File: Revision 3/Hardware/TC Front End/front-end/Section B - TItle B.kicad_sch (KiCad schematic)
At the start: 17 parts, among them J1 Conn_01x02, J2 Conn_01x02, J3 Conn_01x02, U1 LM321, U2 LM321

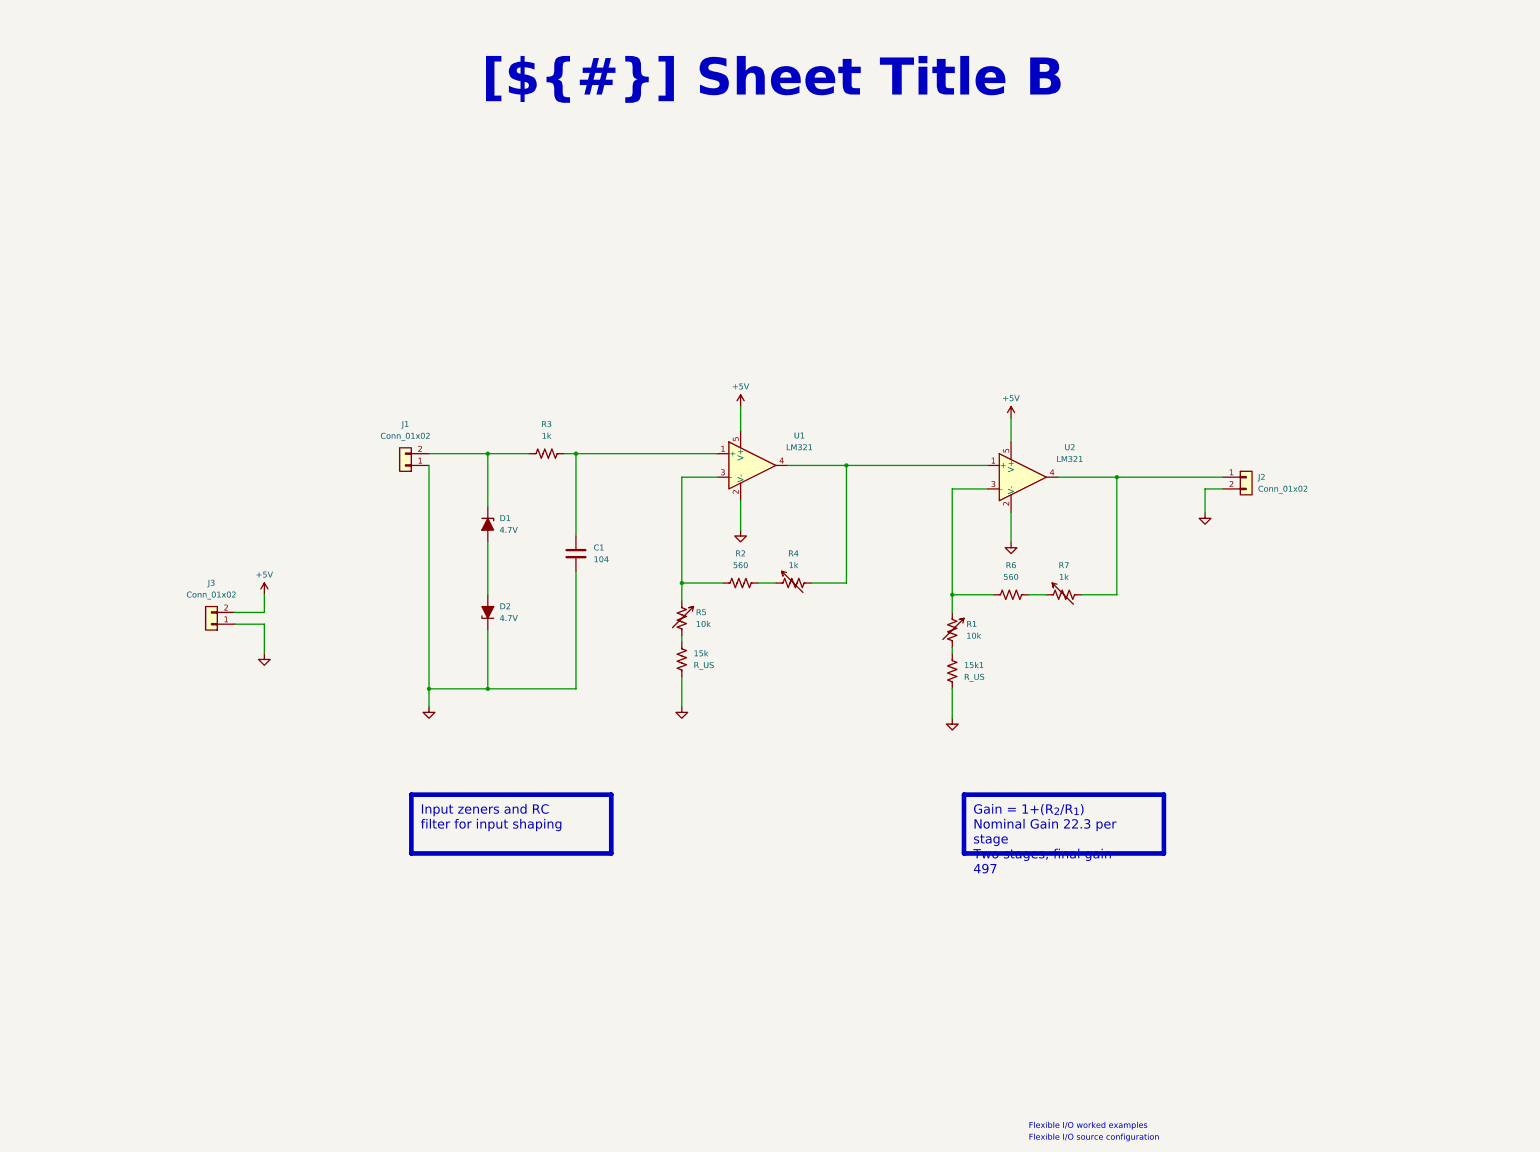
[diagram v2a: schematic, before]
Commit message: Add some notes to the schematic
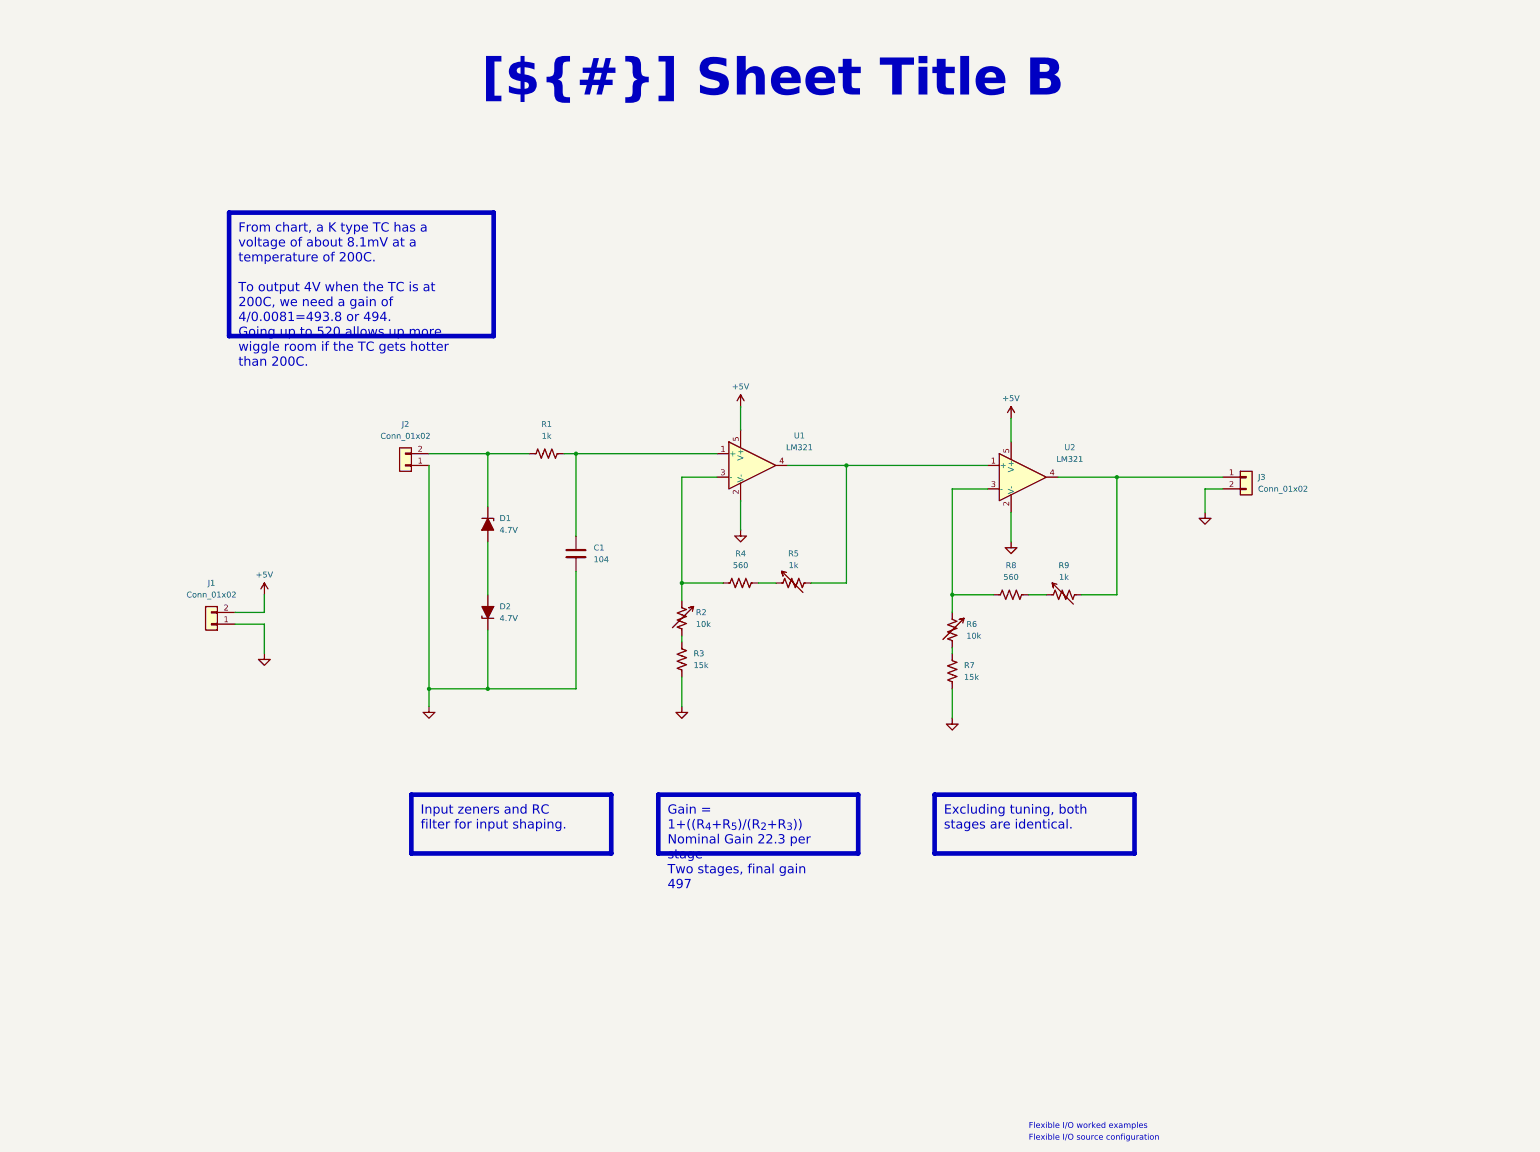
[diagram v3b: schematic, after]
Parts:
- R3: renamed from 15k; value R_US -> 15k
- R7: renamed from 15k1; value R_US -> 15k
- renumbered J3 to J1, J1 to J2, J2 to J3, R3 to R1, R5 to R2, R2 to R4, R4 to R5, R1 to R6, R6 to R8, R7 to R9
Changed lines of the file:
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@@
 		)
 	)
-	(text_box "Gain = 1+(R_{2}/R_{1})\nNominal Gain 22.3 per stage\nTwo stages, final gain 497"
+	(text_box "Gain = 1+((R_{4}+R_{5})/(R_{2}+R_{3}))\nNominal Gain 22.3 per stage\nTwo stages, final gain 497"
 		(exclude_from_sim no)
-		(at 251.46 181.61 0)
+		(at 185.42 181.61 0)
 		(size 43.18 12.7)
 		(margins 2 2 2 2)
@@
 		)
 	)
-	(text_box "Input zeners and RC filter for input shaping"
+	(text_box "Input zeners and RC filter for input shaping."
 		(exclude_from_sim no)
 		(at 132.08 181.61 0)
@@
 		)
 	)
+	(text_box "Excluding tuning, both stages are identical."
+		(exclude_from_sim no)
+		(at 245.11 181.61 0)
+		(size 43.18 12.7)
+		(margins 2 2 2 2)
+		(stroke
+			(width 1)
+			(type solid)
+			(color 200 200 200 1)
+		)
+		(fill
+			(type none)
+		)
+		(effects
+			(font
+				(face "Arial")
+				(size 2 2)
+				(color 0 0 0 1)
+			)
+			(justify left top)
+		)
+	)
 	(text_box "[${#}] ${TITLE}"
 		(exclude_from_sim no)
@@
 		)
 	)
+	(text_box "From chart, a K type TC has a voltage of about 8.1mV at a temperature of 200C.\n\nTo output 4V when the TC is at 200C, we need a gain of 4/0.0081=493.8 or 494.\nGoing up to 520 allows up more wiggle room if the TC gets hotter than 200C."
+		(exclude_from_sim no)
+		(at 92.71 55.88 0)
+		(size 57.15 26.67)
+		(margins 2 2 2 2)
+		(stroke
+			(width 1)
+			(type solid)
+			(color 200 200 200 1)
+		)
+		(fill
+			(type none)
+		)
+		(effects
+			(font
+				(face "Arial")
+				(size 2 2)
+				(color 0 0 0 1)
+			)
+			(justify left top)
+		)
+	)
 	(junction
 		(at 284.48 113.03)
@@
 		(on_board yes)
 		(dnp no)
-		(property "Reference" "#PWR09"
+		(property "Reference" "#PWR01"
 			(at 100.33 142.24 0)
 			(effects
@@
 			(project "front-end"
 				(path "/0650c7a8-acba-429c-9f8e-eec0baf0bc1c/fede4c36-00cc-4d3d-b71c-5243ba232202"
-					(reference "#PWR09")
+					(reference "#PWR01")
 					(unit 1)
 				)
@@
 		(dnp no)
 		(fields_autoplaced yes)
-		(property "Reference" "#PWR04"
+		(property "Reference" "#PWR07"
 			(at 248.92 171.45 0)
 			(effects
@@
 			(project "front-end"
 				(path "/0650c7a8-acba-429c-9f8e-eec0baf0bc1c/fede4c36-00cc-4d3d-b71c-5243ba232202"
-					(reference "#PWR04")
+					(reference "#PWR07")
 					(unit 1)
 				)
@@
 		(on_board yes)
 		(dnp no)
-		(property "Reference" "#PWR01"
+		(property "Reference" "#PWR05"
 			(at 203.2 101.6 0)
 			(effects
@@
 			(project ""
 				(path "/0650c7a8-acba-429c-9f8e-eec0baf0bc1c/fede4c36-00cc-4d3d-b71c-5243ba232202"
-					(reference "#PWR01")
+					(reference "#PWR05")
 					(unit 1)
 				)
@@
 		(dnp no)
 		(fields_autoplaced yes)
-		(property "Reference" "#PWR06"
+		(property "Reference" "#PWR09"
 			(at 261.62 133.35 0)
 			(effects
@@
 			(project "front-end"
 				(path "/0650c7a8-acba-429c-9f8e-eec0baf0bc1c/fede4c36-00cc-4d3d-b71c-5243ba232202"
-					(reference "#PWR06")
+					(reference "#PWR09")
 					(unit 1)
 				)
@@
 		(dnp no)
 		(fields_autoplaced yes)
-		(property "Reference" "#PWR010"
+		(property "Reference" "#PWR02"
 			(at 100.33 157.48 0)
 			(effects
@@
 			(project "front-end"
 				(path "/0650c7a8-acba-429c-9f8e-eec0baf0bc1c/fede4c36-00cc-4d3d-b71c-5243ba232202"
-					(reference "#PWR010")
+					(reference "#PWR02")
 					(unit 1)
 				)
@@
 		(dnp no)
 		(fields_autoplaced yes)
-		(property "Reference" "#PWR08"
+		(property "Reference" "#PWR03"
 			(at 135.89 168.91 0)
 			(effects
@@
 			(project "front-end"
 				(path "/0650c7a8-acba-429c-9f8e-eec0baf0bc1c/fede4c36-00cc-4d3d-b71c-5243ba232202"
-					(reference "#PWR08")
+					(reference "#PWR03")
 					(unit 1)
 				)
@@
 		(dnp no)
 		(fields_autoplaced yes)
-		(property "Reference" "R6"
+		(property "Reference" "R8"
 			(at 261.62 132.08 90)
 			(effects
@@
 			(project "front-end"
 				(path "/0650c7a8-acba-429c-9f8e-eec0baf0bc1c/fede4c36-00cc-4d3d-b71c-5243ba232202"
-					(reference "R6")
+					(reference "R8")
 					(unit 1)
 				)
@@
 		(dnp no)
 		(fields_autoplaced yes)
-		(property "Reference" "R3"
+		(property "Reference" "R1"
 			(at 161.29 101.6 90)
 			(effects
@@
 			(project ""
 				(path "/0650c7a8-acba-429c-9f8e-eec0baf0bc1c/fede4c36-00cc-4d3d-b71c-5243ba232202"
-					(reference "R3")
+					(reference "R1")
 					(unit 1)
 				)
@@
 		(dnp no)
 		(fields_autoplaced yes)
-		(property "Reference" "J3"
+		(property "Reference" "J1"
 			(at 88.9 135.89 0)
 			(effects
@@
 			(project "front-end"
 				(path "/0650c7a8-acba-429c-9f8e-eec0baf0bc1c/fede4c36-00cc-4d3d-b71c-5243ba232202"
-					(reference "J3")
+					(reference "J1")
 					(unit 1)
 				)
@@
 		(on_board yes)
 		(dnp no)
-		(property "Reference" "R1"
+		(property "Reference" "R6"
 			(at 251.968 144.78 0)
 			(effects
@@
 			(project "front-end"
 				(path "/0650c7a8-acba-429c-9f8e-eec0baf0bc1c/fede4c36-00cc-4d3d-b71c-5243ba232202"
-					(reference "R1")
+					(reference "R6")
 					(unit 1)
 				)
@@
 		(dnp no)
 		(fields_autoplaced yes)
-		(property "Reference" "#PWR07"
+		(property "Reference" "#PWR010"
 			(at 303.53 127 0)
 			(effects
@@
 			(project "front-end"
 				(path "/0650c7a8-acba-429c-9f8e-eec0baf0bc1c/fede4c36-00cc-4d3d-b71c-5243ba232202"
-					(reference "#PWR07")
+					(reference "#PWR010")
 					(unit 1)
 				)
@@
 		(dnp no)
 		(fields_autoplaced yes)
-		(property "Reference" "J1"
+		(property "Reference" "J2"
 			(at 130.81 101.6 0)
 			(effects
@@
 			(project ""
 				(path "/0650c7a8-acba-429c-9f8e-eec0baf0bc1c/fede4c36-00cc-4d3d-b71c-5243ba232202"
-					(reference "J1")
+					(reference "J2")
 					(unit 1)
 				)
@@
 		(on_board yes)
 		(dnp no)
-		(property "Reference" "R7"
+		(property "Reference" "R9"
 			(at 273.05 132.08 90)
 			(effects
@@
 			(project "front-end"
 				(path "/0650c7a8-acba-429c-9f8e-eec0baf0bc1c/fede4c36-00cc-4d3d-b71c-5243ba232202"
-					(reference "R7")
+					(reference "R9")
 					(unit 1)
 				)
@@
 		(on_board yes)
 		(dnp no)
-		(property "Reference" "R5"
+		(property "Reference" "R2"
 			(at 193.548 142.24 0)
 			(effects
@@
 			(project "front-end"
 				(path "/0650c7a8-acba-429c-9f8e-eec0baf0bc1c/fede4c36-00cc-4d3d-b71c-5243ba232202"
-					(reference "R5")
+					(reference "R2")
 					(unit 1)
 				)
@@
 		(on_board yes)
 		(dnp no)
-		(property "Reference" "#PWR05"
+		(property "Reference" "#PWR08"
 			(at 261.62 104.14 0)
 			(effects
@@
 			(project "front-end"
 				(path "/0650c7a8-acba-429c-9f8e-eec0baf0bc1c/fede4c36-00cc-4d3d-b71c-5243ba232202"
-					(reference "#PWR05")
+					(reference "#PWR08")
 					(unit 1)
 				)
@@
 		(dnp no)
 		(fields_autoplaced yes)
-		(property "Reference" "15k"
+		(property "Reference" "R3"
 			(at 193.04 151.1299 0)
 			(effects
@@
 			)
 		)
-		(property "Value" "R_US"
+		(property "Value" "15k"
 			(at 193.04 153.6699 0)
 			(effects
@@
 			(project ""
 				(path "/0650c7a8-acba-429c-9f8e-eec0baf0bc1c/fede4c36-00cc-4d3d-b71c-5243ba232202"
-					(reference "15k")
+					(reference "R3")
 					(unit 1)
 				)
@@
 		(dnp no)
 		(fields_autoplaced yes)
-		(property "Reference" "#PWR02"
+		(property "Reference" "#PWR06"
 			(at 203.2 130.81 0)
 			(effects
@@
 			(project ""
 				(path "/0650c7a8-acba-429c-9f8e-eec0baf0bc1c/fede4c36-00cc-4d3d-b71c-5243ba232202"
-					(reference "#PWR02")
+					(reference "#PWR06")
 					(unit 1)
 				)
@@
 		(dnp no)
 		(fields_autoplaced yes)
-		(property "Reference" "J2"
+		(property "Reference" "J3"
 			(at 314.96 113.0299 0)
 			(effects
@@
 			(project "front-end"
 				(path "/0650c7a8-acba-429c-9f8e-eec0baf0bc1c/fede4c36-00cc-4d3d-b71c-5243ba232202"
-					(reference "J2")
+					(reference "J3")
 					(unit 1)
 				)
@@
 		(on_board yes)
 		(dnp no)
-		(property "Reference" "R4"
+		(property "Reference" "R5"
 			(at 214.63 129.54 90)
 			(effects
@@
 			(project ""
 				(path "/0650c7a8-acba-429c-9f8e-eec0baf0bc1c/fede4c36-00cc-4d3d-b71c-5243ba232202"
-					(reference "R4")
+					(reference "R5")
 					(unit 1)
 				)
@@
 		(dnp no)
 		(fields_autoplaced yes)
-		(property "Reference" "R2"
+		(property "Reference" "R4"
 			(at 203.2 129.54 90)
 			(effects
@@
 			(project "front-end"
 				(path "/0650c7a8-acba-429c-9f8e-eec0baf0bc1c/fede4c36-00cc-4d3d-b71c-5243ba232202"
-					(reference "R2")
+					(reference "R4")
 					(unit 1)
 				)
@@
 		(dnp no)
 		(fields_autoplaced yes)
-		(property "Reference" "#PWR03"
+		(property "Reference" "#PWR04"
 			(at 190.5 168.91 0)
 			(effects
@@
 			(project "front-end"
 				(path "/0650c7a8-acba-429c-9f8e-eec0baf0bc1c/fede4c36-00cc-4d3d-b71c-5243ba232202"
-					(reference "#PWR03")
+					(reference "#PWR04")
 					(unit 1)
 				)
@@
 		(dnp no)
 		(fields_autoplaced yes)
-		(property "Reference" "15k1"
+		(property "Reference" "R7"
 			(at 251.46 153.6699 0)
 			(effects
@@
 			)
 		)
-		(property "Value" "R_US"
+		(property "Value" "15k"
 			(at 251.46 156.2099 0)
 			(effects
@@
 			(project "front-end"
 				(path "/0650c7a8-acba-429c-9f8e-eec0baf0bc1c/fede4c36-00cc-4d3d-b71c-5243ba232202"
-					(reference "15k1")
+					(reference "R7")
 					(unit 1)
 				)

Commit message: Add references
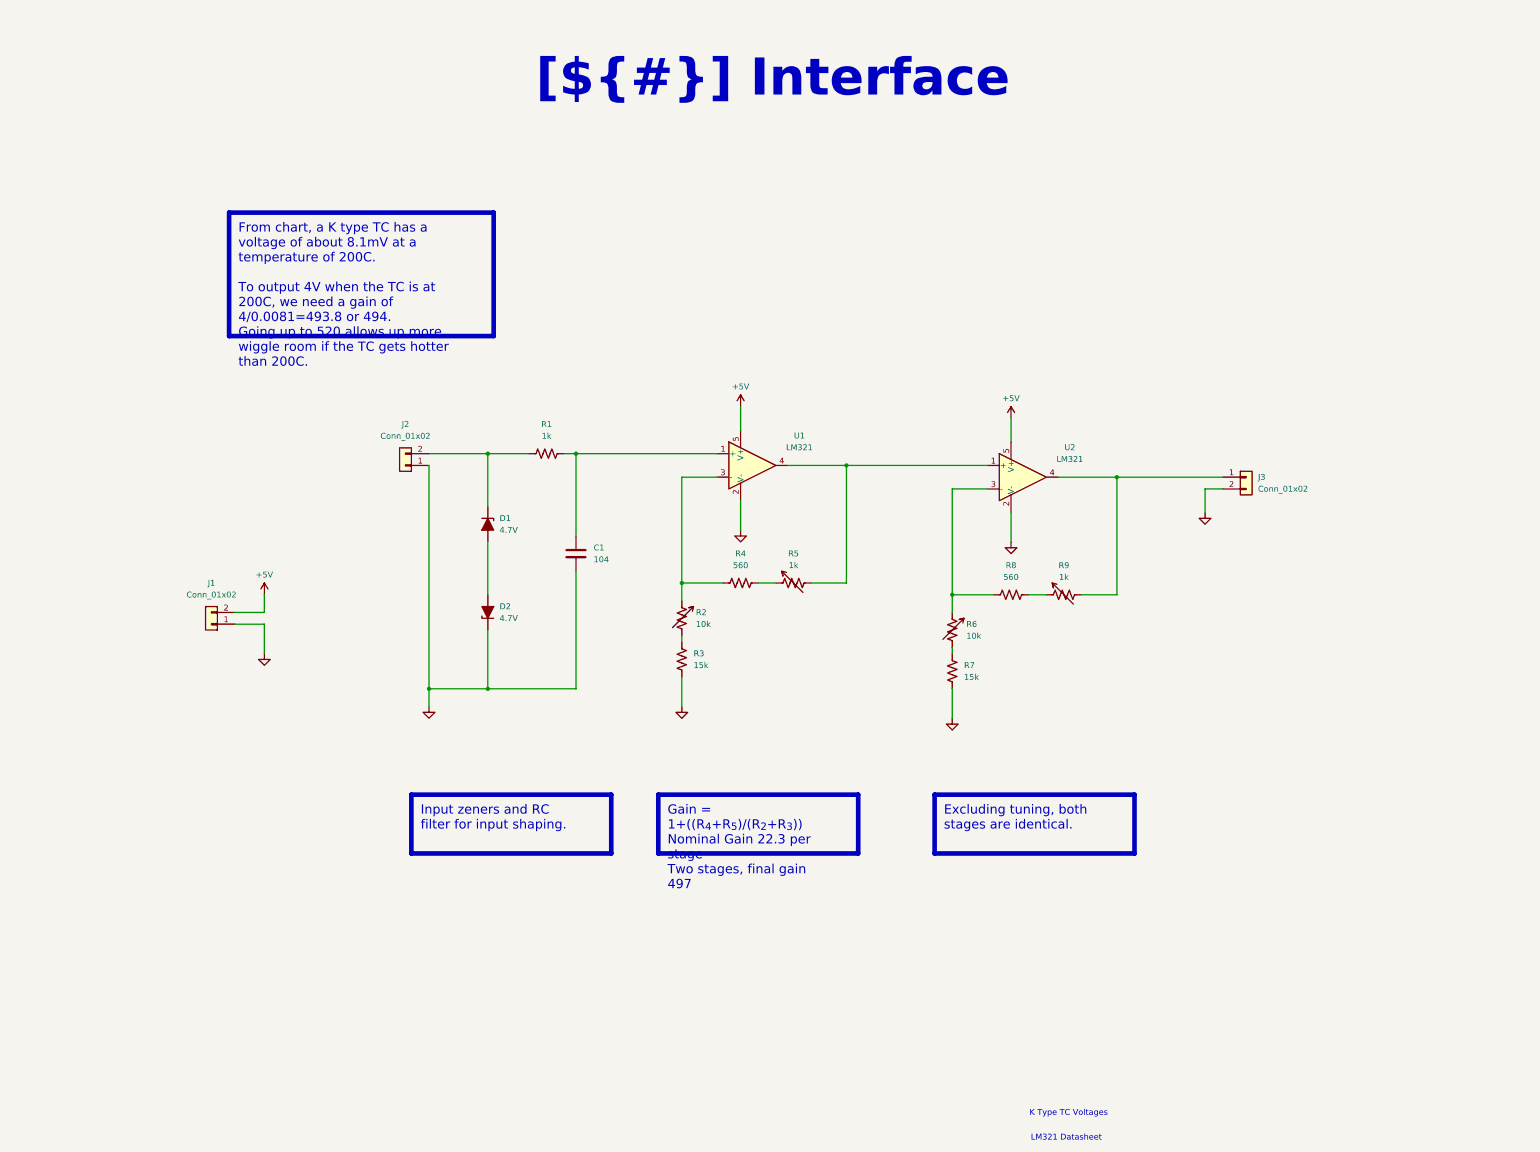
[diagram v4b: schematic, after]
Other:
- note added: "K Type TC Voltages"
- note added: "LM321 Datasheet"
- note removed: "Flexible I/O source configuration"
- note removed: "Flexible I/O worked examples"
- title: Sheet Title B -> Interface
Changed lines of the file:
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@@
 	(paper "A3")
 	(title_block
-		(title "Sheet Title B")
+		(title "Interface")
 		(date "Last Modified Date")
 		(rev "${REVISION}")
 		(company "${COMPANY}")
 	)
-	(text "Flexible I/O worked examples"
+	(text "K Type TC Voltages"
 		(exclude_from_sim no)
-		(at 265.43 254 0)
+		(at 274.066 250.444 0)
 		(effects
 			(font
-				(face "Arial")
 				(size 1.27 1.27)
-				(color 0 0 0 1)
 			)
-			(justify left bottom)
-			(href "https://jpieper.com/2022/06/30/flexible-i-o-worked-examples/")
+			(href "https://www.pyromation.com/downloads/data/emfk_c.pdf")
 		)
 	)
-	(text "Flexible I/O source configuration"
+	(text "LM321 Datasheet"
 		(exclude_from_sim no)
-		(at 265.43 256.54 0)
+		(at 273.558 255.778 0)
 		(effects
 			(font
-				(face "Arial")
 				(size 1.27 1.27)
-				(color 0 0 0 1)
 			)
-			(justify left bottom)
-			(href "https://jpieper.com/2022/06/28/flexible-i-o-source-configuration/")
+			(href "https://www.onsemi.com/pdf/datasheet/lm321-d.pdf")
 		)
 	)
